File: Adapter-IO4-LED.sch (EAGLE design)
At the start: 7 parts

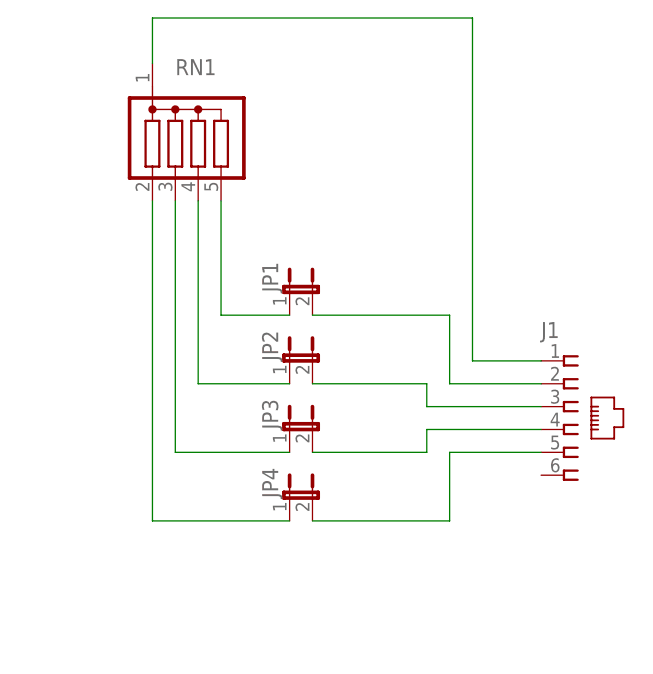
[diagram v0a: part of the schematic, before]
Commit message: added values for connectors
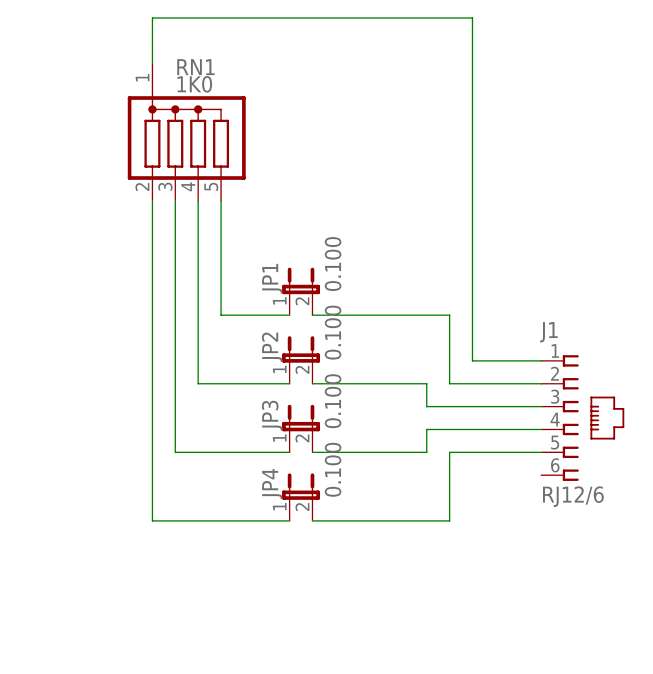
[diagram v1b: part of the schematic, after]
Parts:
- J1: value (none) -> RJ12/6
- JP1, JP2, JP3, JP4: value (none) -> 0.100
- RN1: value (none) -> 1K0
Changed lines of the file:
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@@
 <part name="FRAME1" library="SparkFun" deviceset="FRAME-LETTER" device=""/>
 <part name="U$1" library="SPCoast" deviceset="DOC-OSHW-LOGO-" device="M"/>
-<part name="J1" library="SPCoast" deviceset="CONNECTOR-RJ25" device="-6P6C"/>
-<part name="JP1" library="SPCoast" deviceset="JUMPER-2" device="PTH_LOCK"/>
-<part name="JP2" library="SPCoast" deviceset="JUMPER-2" device="PTH_LOCK"/>
-<part name="JP3" library="SPCoast" deviceset="JUMPER-2" device="PTH_LOCK"/>
-<part name="JP4" library="SPCoast" deviceset="JUMPER-2" device="PTH_LOCK"/>
-<part name="RN1" library="resistor-sil" deviceset="G04R" device=""/>
+<part name="J1" library="SPCoast" deviceset="CONNECTOR-RJ25" device="-6P6C" value="RJ12/6"/>
+<part name="JP1" library="SPCoast" deviceset="JUMPER-2" device="PTH_LOCK" value="0.100"/>
+<part name="JP2" library="SPCoast" deviceset="JUMPER-2" device="PTH_LOCK" value="0.100"/>
+<part name="JP3" library="SPCoast" deviceset="JUMPER-2" device="PTH_LOCK" value="0.100"/>
+<part name="JP4" library="SPCoast" deviceset="JUMPER-2" device="PTH_LOCK" value="0.100"/>
+<part name="RN1" library="resistor-sil" deviceset="G04R" device="" value="1K0"/>
 </parts>
 <sheets>

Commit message: normalized values
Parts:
- U$1: value DOC-OSHW-LOGO-M -> OSHW
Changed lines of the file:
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@@
 <parts>
 <part name="FRAME1" library="SparkFun" deviceset="FRAME-LETTER" device=""/>
-<part name="U$1" library="SPCoast" deviceset="DOC-OSHW-LOGO-" device="M"/>
+<part name="U$1" library="SPCoast" deviceset="DOC-OSHW-LOGO-" device="M" value="OSHW"/>
 <part name="J1" library="SPCoast" deviceset="CONNECTOR-RJ25" device="-6P6C" value="RJ12/6"/>
 <part name="JP1" library="SPCoast" deviceset="JUMPER-2" device="PTH_LOCK" value="0.100"/>
